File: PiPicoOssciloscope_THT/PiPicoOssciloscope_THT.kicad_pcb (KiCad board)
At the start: 2 copper layers, 100 x 100 mm, 84 parts, among them J1 Conn_Coaxial, J2 Conn_Coaxial, U1 SMQS-04R-TP, U2 SMQS-04R-TP, U3 SMQS-04R-TP, U4 SMQS-04R-TP, U5 SMQS-04R-TP, U6 SMQS-04R-TP, U7 SMQS-04R-TP, U8 MCP6002-I/P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

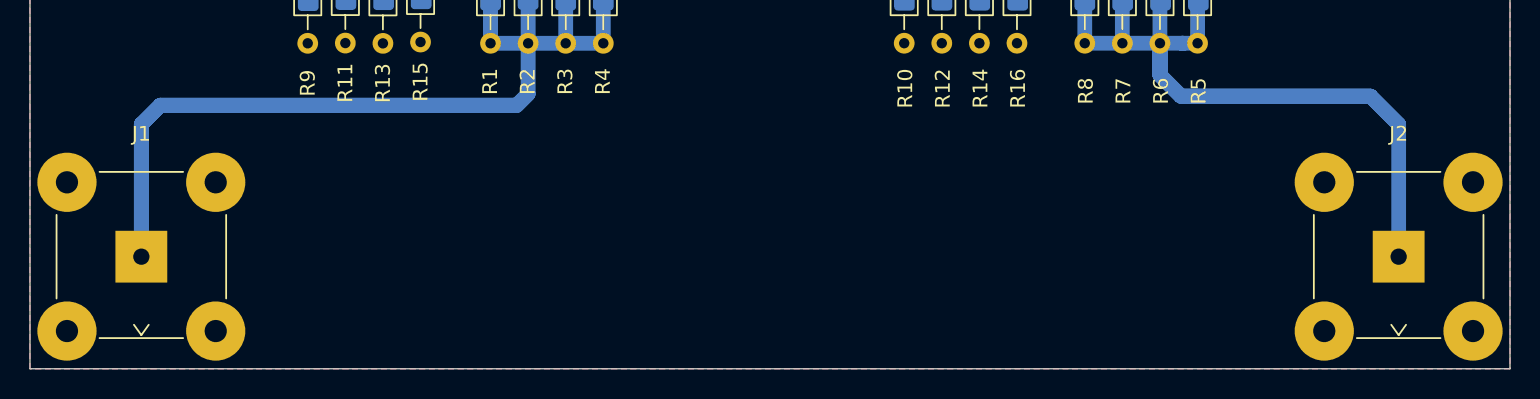
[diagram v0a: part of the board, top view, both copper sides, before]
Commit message: updated the bnc connector
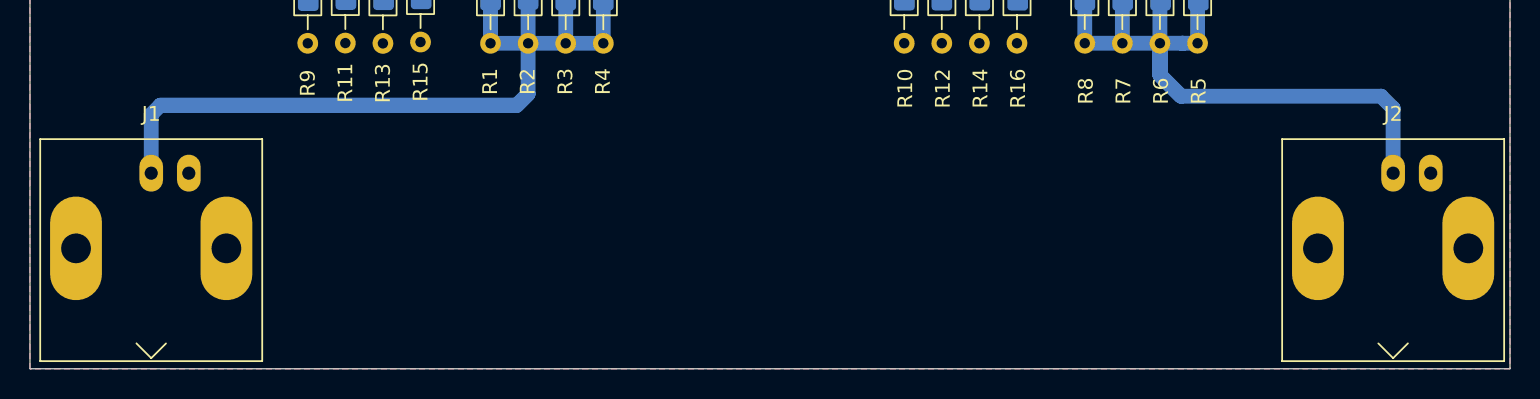
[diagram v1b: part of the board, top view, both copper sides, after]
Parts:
- J1, J2: footprint Connector_Coaxial:BNC_TEConnectivity_1478035_Horizontal -> Connector_Coaxial:BNC_Amphenol_B6252HB-NPP3G-50_Horizontal
- moved J1 5.68 mm to (150.6, 123.5)
- moved J2 5.66 mm to (234.5, 123.5)
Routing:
- net /Input/CH2: track 84.2 -> 50.9 mm
- net /Input/CH1: track 94.2 -> 77.6 mm
